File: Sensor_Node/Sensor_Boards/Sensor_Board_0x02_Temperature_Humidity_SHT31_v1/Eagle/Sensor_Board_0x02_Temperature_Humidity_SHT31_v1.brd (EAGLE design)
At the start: 55 x 35 mm, 16 parts, among them J1 M04_SMD_90, J4 ARDUINO_ISP, U2 ATMEGA328P_TQFP, Y1 8MHZ

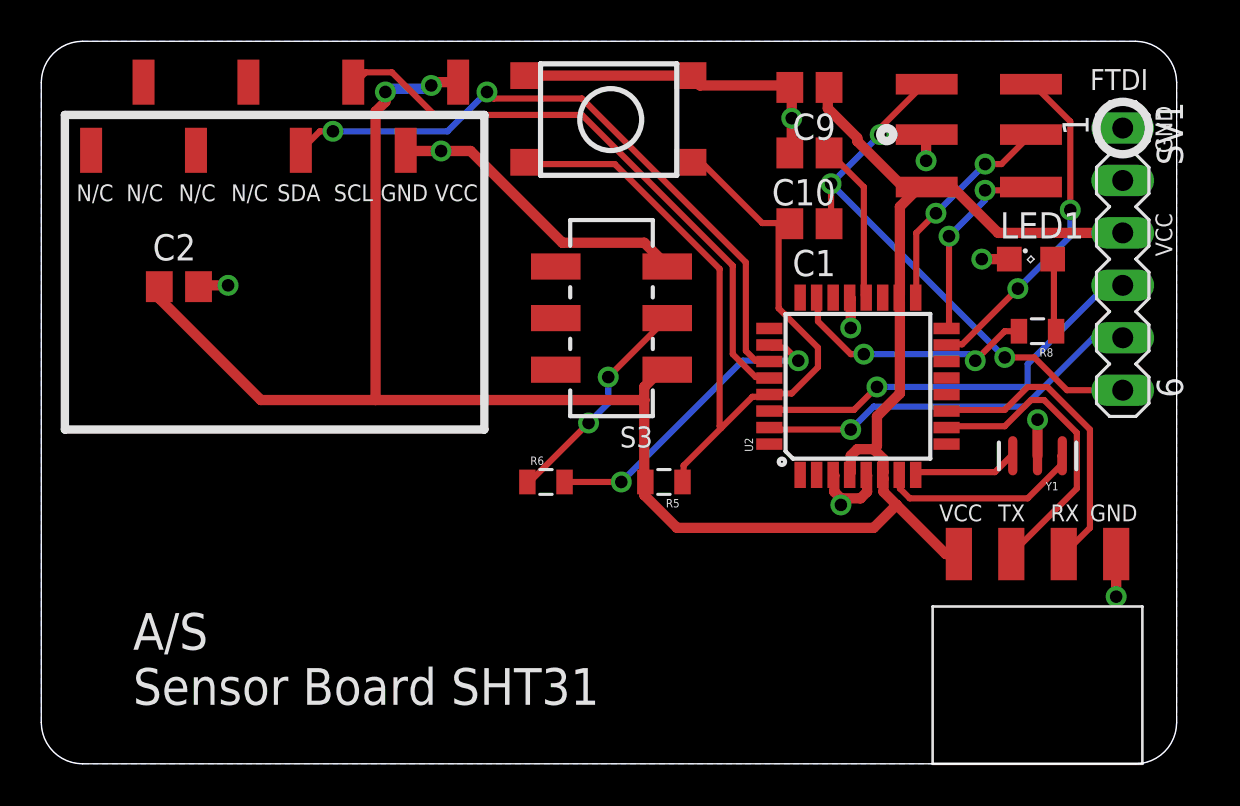
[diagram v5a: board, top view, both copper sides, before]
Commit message: SHT31
- reset path
- sensor connector footer
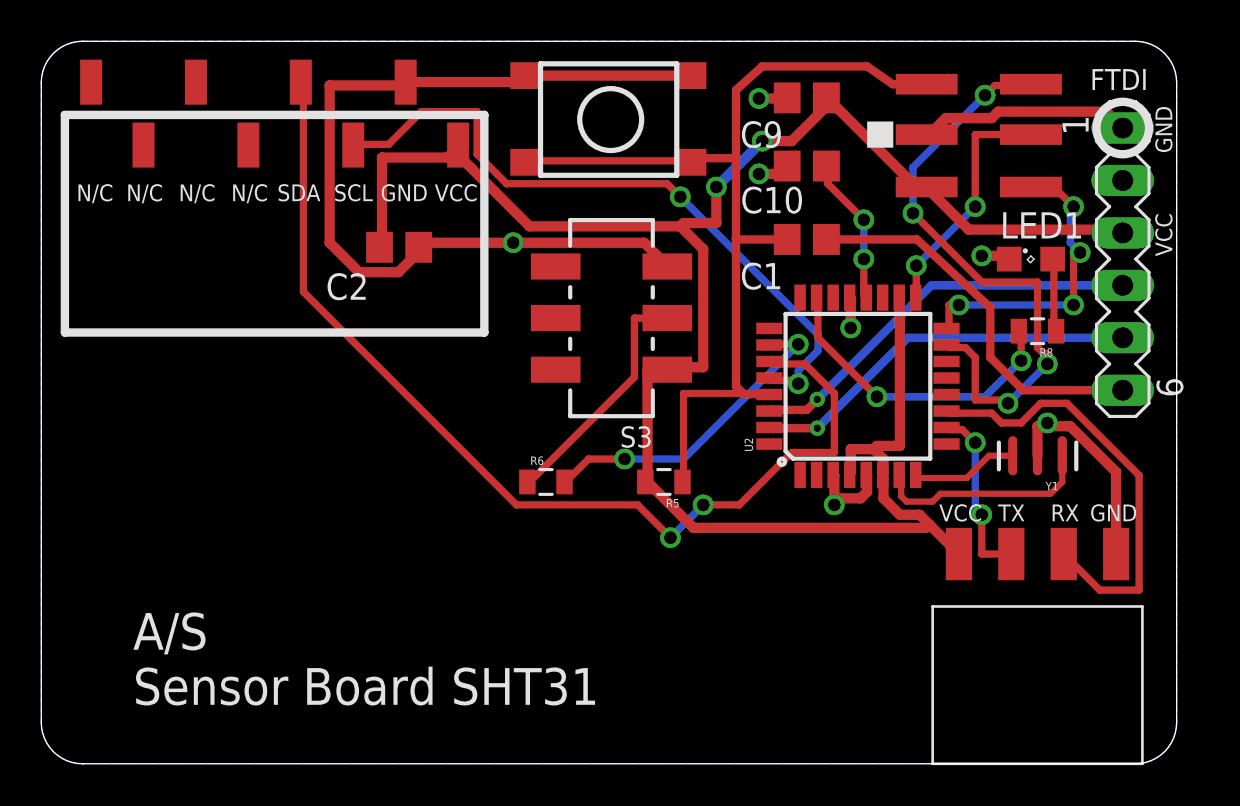
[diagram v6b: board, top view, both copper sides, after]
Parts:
- removed U$20: M08_SMD_STRAIGHT, myownthings:M08_SMD_STRAIGHT
- added U$9: M08_SMD_STRAIGHT, wsn:M08_SMD_STRAIGHT
- moved C2 10.8 mm to (17.3, 25.0)
- moved C1 0.77 mm to (37.1, 25.4)
- moved C10 0.65 mm to (37.1, 29.0)
- moved C9 0.52 mm to (37.1, 32.3)
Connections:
- removed net N$4: C1.2, R5.1, S1.3, S1.4, U2.29
- new net FTDI_RESET: C1.1, SV1.6
- net GND: now also U$9.P7; no longer U$20.P7
- net RESET: now also C1.2, R5.1, S1.3, S1.4, U2.29; no longer C1.1, SV1.6
- net SCL: now also U$9.P6; no longer U$20.P6
- net SDA: now also U$9.P5; no longer U$20.P5
- net VCC: now also U$9.P8; no longer U$20.P8
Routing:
- net N$4: track 43.0 -> 0.00 mm
- net GND: track 44.6 -> 73.8 mm, vias 9 -> 7
- net RESET: track 27.3 -> 46.6 mm, vias 3 -> 0
- net FTDI_RESET: track 0.00 -> 18.7 mm
- net SDA: track 31.8 -> 49.3 mm
- net MOSI: track 16.5 -> 29.4 mm, vias 2 -> 4
- net VCC: track 106.6 -> 97.7 mm
- net MCU_RXI: track 14.8 -> 21.3 mm
- net MCU_TXO: track 14.7 -> 8.64 mm, vias 0 -> 2
- net MISO: track 9.80 -> 15.1 mm, vias 2 -> 4
- net SCL: track 29.0 -> 33.1 mm, vias 0 -> 2
- net L1: track 12.3 -> 15.3 mm
- net SCK: track 10.7 -> 11.8 mm
- net N$3: track 10.8 -> 11.7 mm, vias 2 -> 0
- net N$2: track 9.87 -> 10.7 mm
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
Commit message: Started tidying of SHT31
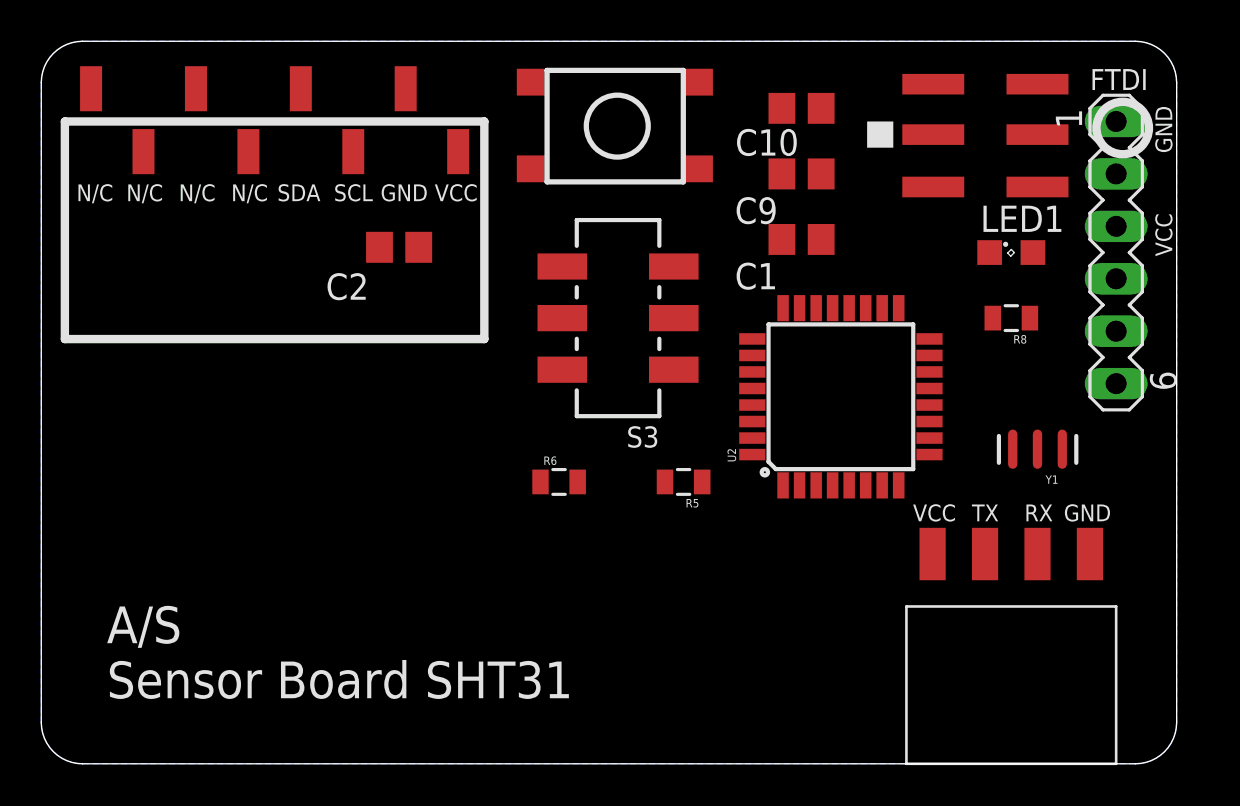
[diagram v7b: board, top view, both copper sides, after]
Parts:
- moved C9 3.69 mm to (36.8, 28.6)
- moved C10 2.81 mm to (36.8, 31.8)
- moved R8 1.42 mm to (47.0, 21.6)
- moved J1 1.27 mm to (43.2, 10.2)
- moved LED1 1.00 mm to (47.0, 24.8)
- moved U2 0.97 mm to (38.7, 17.8)
- moved R5 0.95 mm to (31.1, 13.7)
- moved R6 0.63 mm to (25.1, 13.7)
- moved SV1 0.45 mm to (52.1, 24.8)
- moved S1 0.45 mm to (23.8, 33.0)
- moved S3 0.32 mm to (27.9, 21.6)
- moved U$9 0.32 mm to (2.41, 32.7)
- moved Y1 0.32 mm to (48.3, 15.2)
- moved J4 0.32 mm to (48.3, 27.9)
- moved C1 0.25 mm to (36.8, 25.4)
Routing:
- net VCC: track 97.7 -> 0.00 mm, vias 2 -> 0
- net GND: track 73.8 -> 0.00 mm, vias 7 -> 0
- net SDA: track 49.3 -> 0.00 mm, vias 2 -> 0
- net RESET: track 46.6 -> 0.00 mm
- net SCL: track 33.1 -> 0.00 mm, vias 2 -> 0
- net MOSI: track 29.4 -> 0.00 mm, vias 4 -> 0
- net MCU_RXI: track 21.3 -> 0.00 mm
- net FTDI_RXI: track 19.6 -> 0.00 mm, vias 1 -> 0
- net FTDI_TXO: track 18.9 -> 0.00 mm, vias 1 -> 0
- net FTDI_RESET: track 18.7 -> 0.00 mm
- net DBG_ENABLE: track 15.5 -> 0.00 mm, vias 2 -> 0
- net L1: track 15.3 -> 0.00 mm, vias 2 -> 0
- net MISO: track 15.1 -> 0.00 mm, vias 4 -> 0
- net SCK: track 11.8 -> 0.00 mm, vias 2 -> 0
- net N$3: track 11.7 -> 0.00 mm
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
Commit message: Update SHT31
- only descriptions missing
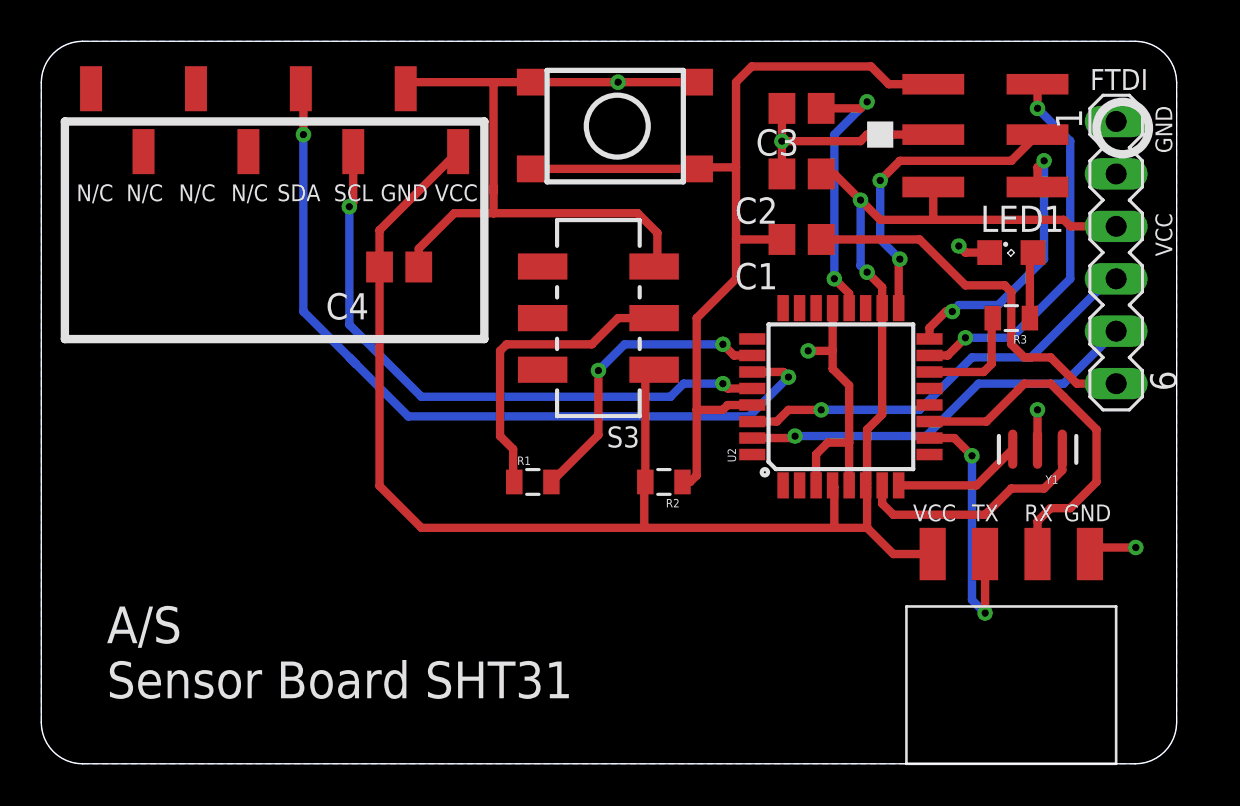
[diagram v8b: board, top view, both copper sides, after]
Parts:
- removed C9: 100n, eagle-ltspice:C0805
- removed R5, R6: 10k, SparkFun-Passives:0805
- added C4: 100n, eagle-ltspice:C0805
- added R1, R2: 10k, SparkFun-Passives:0805
- moved C2 19.8 mm to (36.8, 28.6), turned to 180 degrees
- moved S3 0.95 mm to (27.0, 21.6)
- renumbered C10 to C3, R8 to R3
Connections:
- net DBG_ENABLE: now also R1.2; no longer R6.2
- net GND: now also C4.2; no longer C9.2
- net L1: now also U2.14; no longer U2.23
- net N$3: now also R1.1; no longer R6.1
- net RESET: now also R2.1; no longer R5.1
- net VCC: now also C4.1, R2.2; no longer C9.1, R5.2
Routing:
- net VCC: track 0.00 -> 89.5 mm, vias 0 -> 2
- net GND: track 0.00 -> 66.1 mm, vias 0 -> 6
- net RESET: track 0.00 -> 45.8 mm
- net SDA: track 0.00 -> 39.5 mm, vias 0 -> 2
- net SCL: track 0.00 -> 29.8 mm, vias 0 -> 2
- net FTDI_RXI: track 0.00 -> 20.5 mm, vias 0 -> 1
- net FTDI_TXO: track 0.00 -> 19.8 mm, vias 0 -> 1
- net FTDI_RESET: track 0.00 -> 18.7 mm
- net MOSI: track 0.00 -> 18.4 mm, vias 0 -> 2
- net MCU_RXI: track 0.00 -> 17.5 mm
- net SCK: track 0.00 -> 15.1 mm, vias 0 -> 2
- net N$3: track 0.00 -> 14.8 mm
- net DBG_ENABLE: track 0.00 -> 14.5 mm, vias 0 -> 2
- net MISO: track 0.00 -> 13.6 mm, vias 0 -> 2
- net N$15: track 0.00 -> 13.3 mm, vias 0 -> 2
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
